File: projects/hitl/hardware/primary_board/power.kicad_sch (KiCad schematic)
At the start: 19 parts, among them J20 CONN_01X03, U1 PCA9517, U9 LT3045

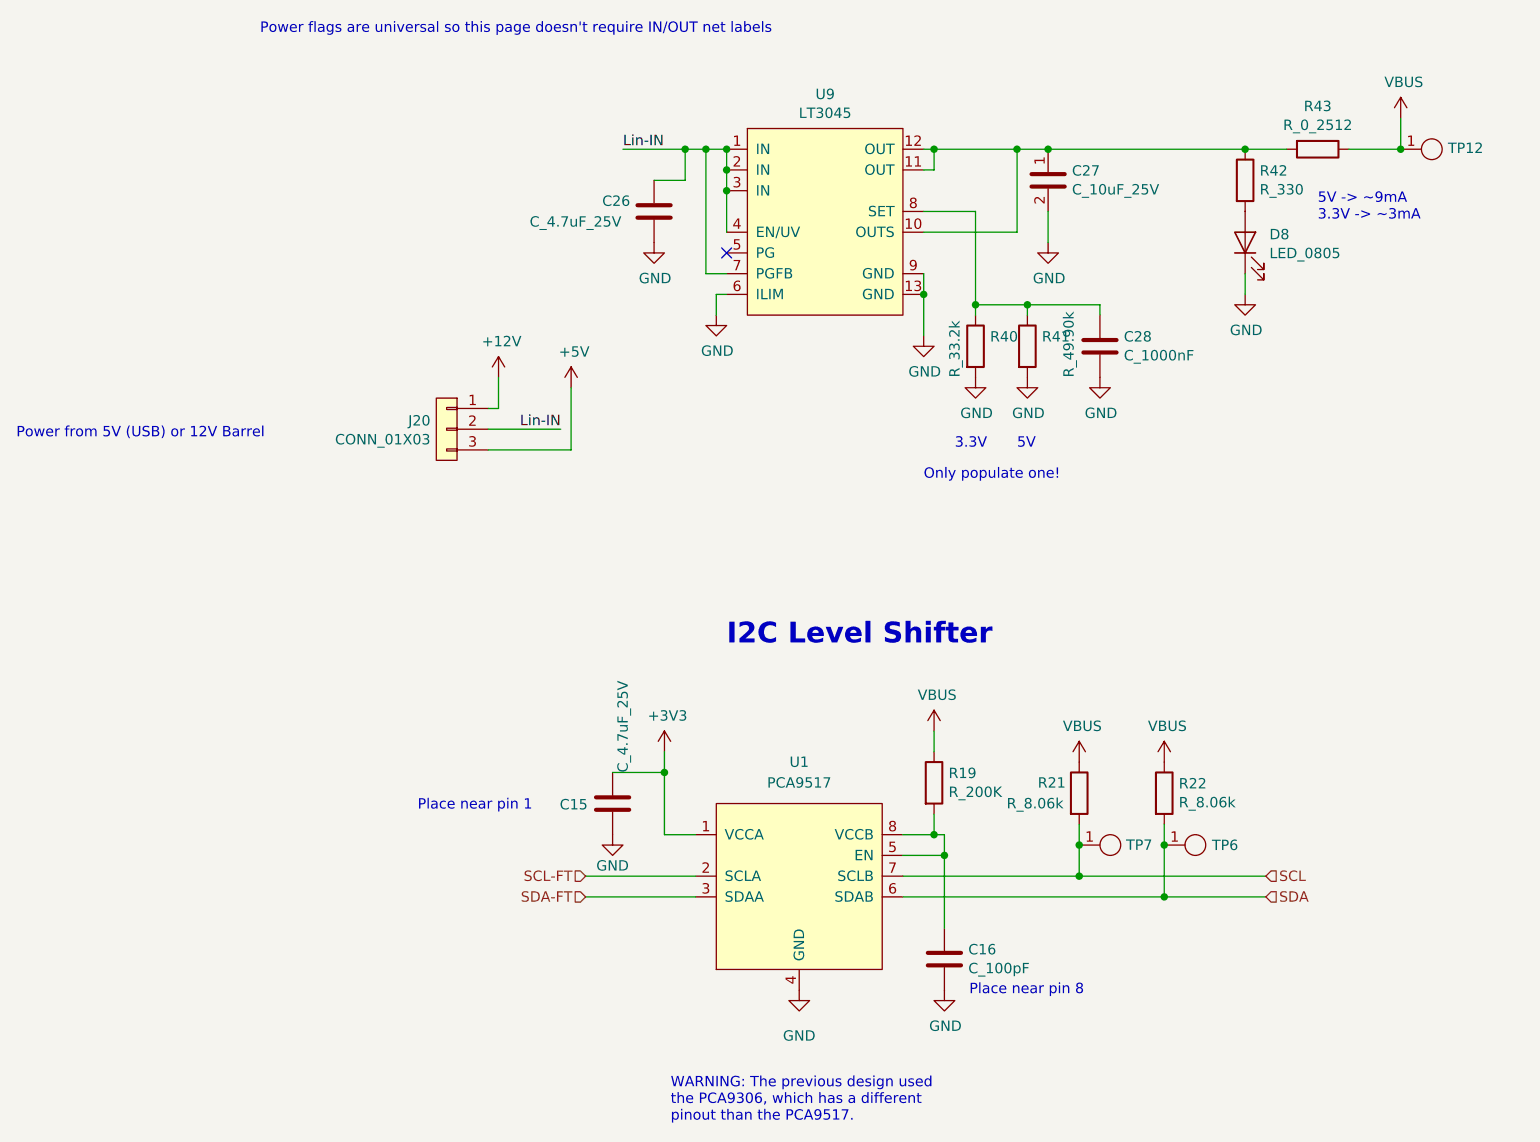
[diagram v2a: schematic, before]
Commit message: spec parts for hitl
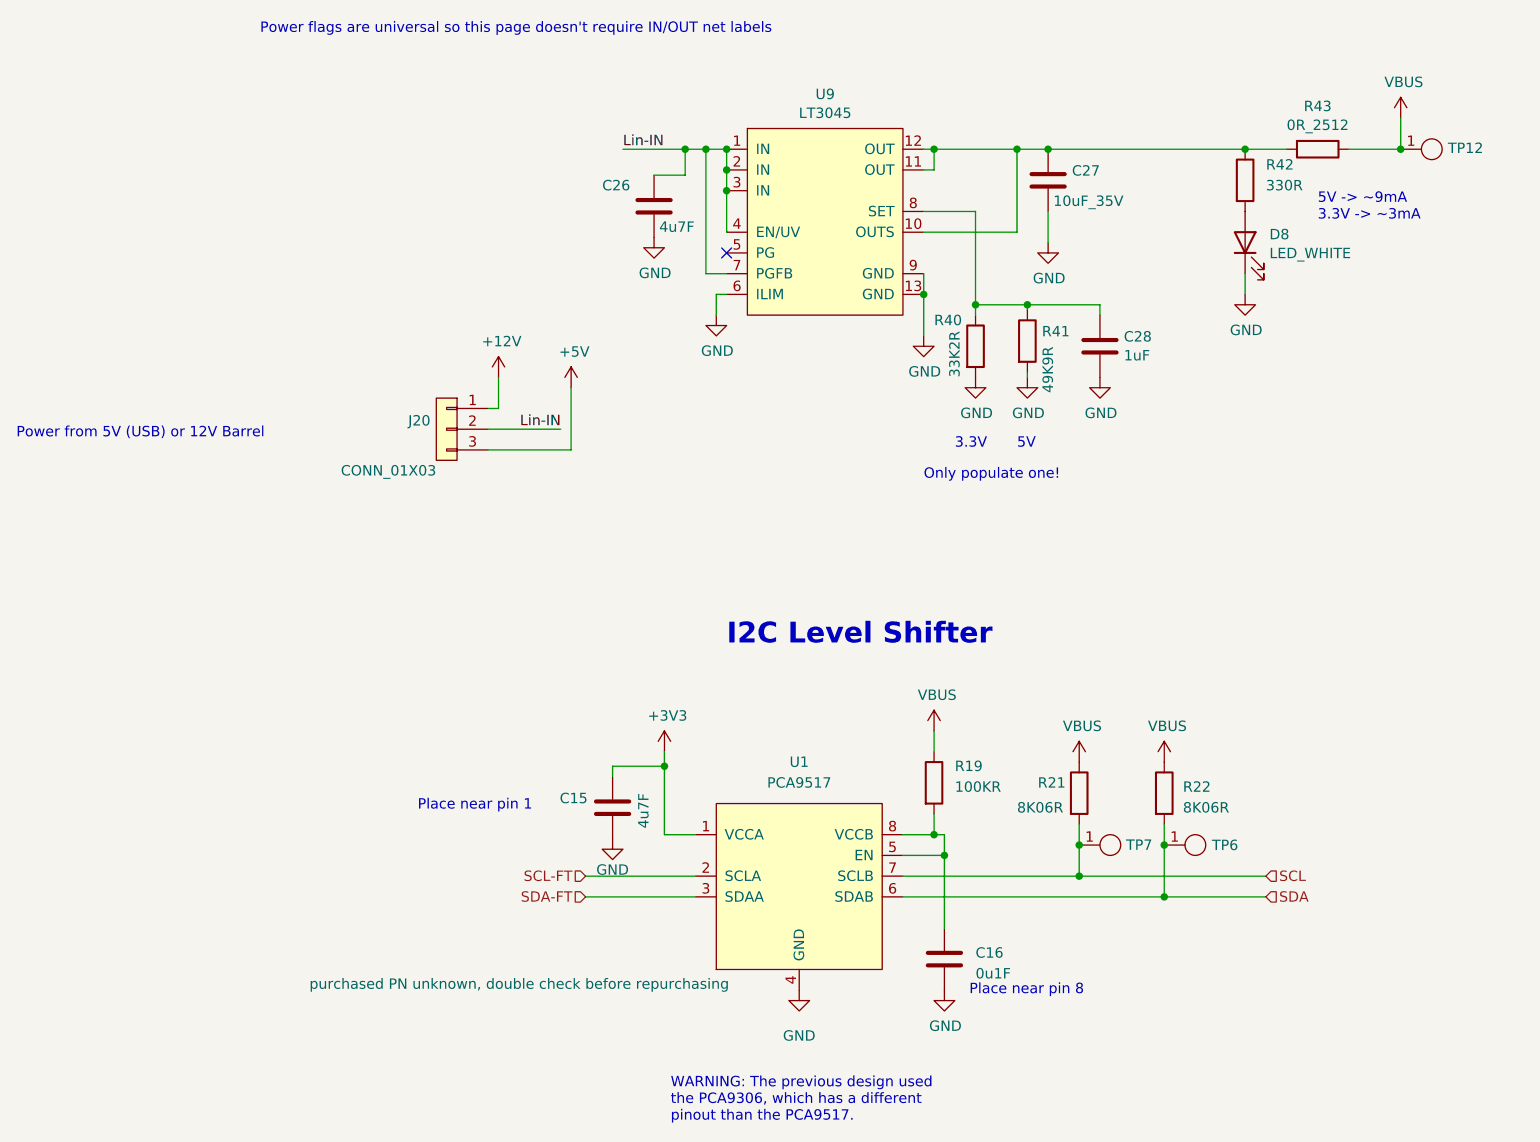
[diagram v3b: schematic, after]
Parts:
- C15, C26: value C_4.7uF_25V -> 4u7F; footprint footprints:C_0805_OEM -> OEM:C_0603; symbol formula:C_4.7uF_25V -> OEM:4u7F; DKPN (none) -> 490-12329-6-ND; MFN (none) -> Murata; MPN (none) -> GRT188R61E475ME13D; NewDesigns (none) -> YES; Package (none) -> 0603; PurchasingLink https://www.digikey.com/product-detail/en/tdk-corporation/C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 -> (none); Stocked (none) -> Digi-Reel; Style (none) -> SMD
- C16: value C_100pF -> 0u1F; footprint footprints:C_0805_OEM -> OEM:C_0603; symbol formula:C_100pF -> OEM:0u1F; DKPN (none) -> 1276-1935-2-ND; MFN DK -> Samsung Electro-Mechanics; MPN 732-7852-1-ND -> CL10B104KB8NNWC; NewDesigns (none) -> YES; Package (none) -> 0603; PurchasingLink https://www.digikey.com/product-detail/en/wurth-electronics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 -> (none); Stocked (none) -> Reel; Style (none) -> SMD
- C27: value C_10uF_25V -> 10uF_35V; footprint footprints:C_0805_OEM -> OEM:C_0603; symbol formula:C_10uF_25V -> OEM:10uF_35V; DKPN (none) -> 490-GRM188R6YA106MA73JDKR-ND; MFN (none) -> Murata; MPN (none) -> GRM188R6YA106MA73J; NewDesigns (none) -> YES; Package (none) -> 0603; Purchasing Link https://www.digikey.com/product-detail/en/murata-electronic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 -> (none); Stocked (none) -> Digi-Reel; Style (none) -> SMD
- C28: value C_1000nF -> 1uF; footprint footprints:C_0603_1608Metric -> OEM:C_0603; symbol formula:C_1000nF -> OEM:1uF; DKPN (none) -> 1276-1184-2-ND; MFN DK -> Samsung Electro-Mechanics; MPN 1276-1946-1-ND -> CL10B105KA8NNNC; NewDesigns (none) -> YES; Package (none) -> 0603; PurchasingLink https://www.digikey.com/product-detail/en/samsung-electro-m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 -> (none); Stocked (none) -> Reel; Style (none) -> SMD
- D8: value LED_0805 -> LED_WHITE; footprint footprints:LED_0805_OEM -> OEM:CHIPLED_0805; symbol formula:LED_0805 -> OEM:LED_WHITE; DKPN (none) -> 3147-B1701TW--20P000314U1930DKR-ND; MFN DK -> Harvatek; MPN 475-1410-1-ND -> B1701TW--20P000314U1930; NewDesigns (none) -> Yes; Package (none) -> 0805; PurchasingLink https://www.digikey.com/products/en?keywords=475-1410-1-ND -> (none); Stocked (none) -> Digi-Reel; Style (none) -> SMD
- J20: symbol formula:CONN_01X03 -> OEM:CONN_01X03; DKPN (none) -> 2057-PH1-03-UA-ND; MFN Mouser -> Adam Tech; MPN 855-M20-9990346 -> PH1-03-UA; NewDesigns (none) -> YES; Package (none) -> .1" pin header; PurchasingLink https://www.mouser.com/ProductDetail/Harwin/M20-9990346?qs=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 -> (none); Stocked (none) -> Bulk; Style (none) -> THT
- R19: value R_200K -> 100KR; footprint footprints:R_0805_OEM -> OEM:R_0603; symbol formula:R_200K -> OEM:100KR; DKPN (none) -> RMCF0603FT100KTR-ND; MFN DK -> Stackpole Electronics; MPN P300KDACT-ND -> RMCF0603FT100K; NewDesigns (none) -> YES; Package (none) -> 0603; Stocked (none) -> Reel; Style (none) -> SMD
- R21, R22: value R_8.06k -> 8K06R; footprint footprints:R_0805_OEM -> OEM:R_0603; symbol formula:R_8.06k -> OEM:8K06R; DKPN (none) -> RMCF0603FT8K06DKR-ND; MFN TE -> Stackpole Electronics; MPN RQ73C2A8K06BTD -> RMCF0603FT8K06; NewDesigns (none) -> YES; Package (none) -> 0603; PurchasingLink https://www.digikey.com/en/products/detail/te-connectivity-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 -> (none); Stocked (none) -> Digi-Reel; Style (none) -> SMD
- R40: value R_33.2k -> 33K2R; footprint footprints:R_0805_OEM -> OEM:R_0603; symbol formula:R_33.2k -> OEM:33K2R; DKPN (none) -> RMCF0603FT33K2DKR-ND; MFN TE -> Stackpole Electronics; MPN 5-2176093-2 -> RMCF0603FT33K2; NewDesigns (none) -> YES; Package (none) -> 0603; PurchasingLink https://www.digikey.com/en/products/detail/te-connectivity-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 -> (none); Stocked (none) -> Digi-Reel; Style (none) -> SMD
- R41: value R_49.90k -> 49K9R; footprint footprints:R_0805_OEM -> OEM:R_0603; symbol formula:R_49.90k -> OEM:49K9R; DKPN (none) -> RMCF0603FT39K0TR-ND; MFN Panasonic -> Stackpole Electronics; MPN ERA-6AEB4992V -> RMCF0603FT39K0; NewDesigns (none) -> YES; Package (none) -> 0603; PurchasingLink https://www.digikey.com/en/products/detail/panasonic-electr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 -> (none); Stocked (none) -> Reel; Style (none) -> SMD
- R42: value R_330 -> 330R; footprint footprints:R_0805_OEM -> OEM:R_0603; symbol formula:R_330 -> OEM:330R; DKPN (none) -> 1292-WR06X3300FTLDKR-ND; MFN DK -> Walsin; MPN RMCF0805FT330RCT-ND -> WR06X3300FTL; NewDesigns (none) -> YES; Package (none) -> 0603; PurchasingLink https://www.digikey.com/product-detail/en/stackpole-electro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 -> (none); Stocked (none) -> Digi-Reel; Style (none) -> SMD
- R43: value R_0_2512 -> 0R_2512; footprint footprints:R_2512_OEM -> Resistor_SMD:R_2512_6332Metric; symbol formula:R_0_2512 -> OEM:0R_2512; DKPN (none) -> CR2512-J/-000ELFCT-ND; MFN DK -> Stackpole Electronics; MPN A121322CT-ND -> CR2512-J/-000ELF; NewDesigns (none) -> YES; Package (none) -> 2512; PurchasingLink https://www.digikey.com/products/en?keywords=A121322CT-ND -> (none); Stocked (none) -> Tape; Style (none) -> SMD
- TP12, TP6, TP7: value Test_Point_SMD -> TP_SMD; symbol formula:Test_Point_SMD -> OEM:TP_SMD; DKPN (none) -> 36-5019TR-ND; MFN (none) -> Keystone; MPN (none) -> 5019; NewDesigns (none) -> YES; Package (none) -> Custom; Stocked (none) -> Reel; Style (none) -> SMD
- U1: MFN onsemi -> TI; MPN PCA9517ADMR2G -> PCA9306DCUTG4; NOTE (none) -> purchased PN unknown, double check before repurchasing; PurchasingLink https://www.mouser.com/ProductDetail/onsemi/PCA9517ADMR2G?q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 -> https://www.digikey.com/en/products/detail/texas-instrument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
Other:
- moved on the sheet: C15, C26, R41
